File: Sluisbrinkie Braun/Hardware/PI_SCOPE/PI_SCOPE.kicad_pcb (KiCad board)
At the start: 2 copper layers, 40 x 110 mm, 97 parts, among them J1 Eurorack Power, J10 CV4, J2 USB_C_Receptacle_USB2.0_16P, J3 CV1, J4 CV2, J5 CV3, J6 CV4, J7 CV1, J8 CV2, J9 CV3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

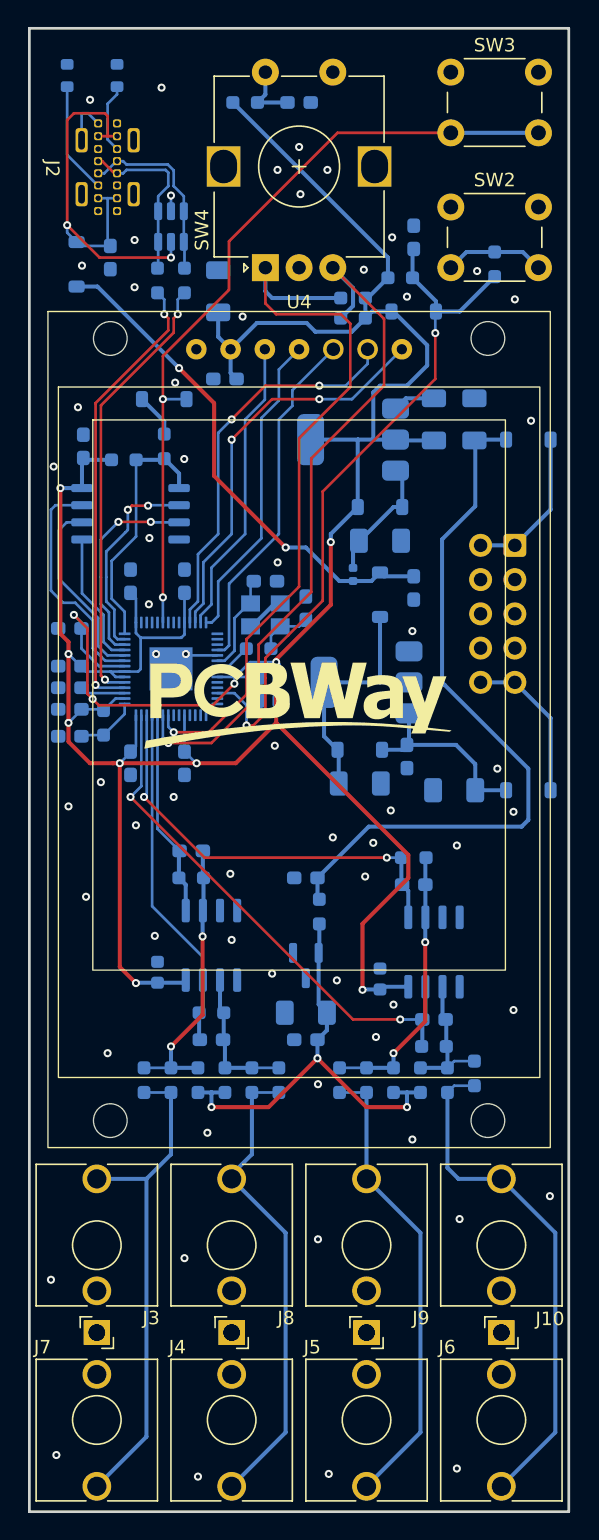
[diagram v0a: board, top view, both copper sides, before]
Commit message: [Braun] Several hardware fixes, move display from SPI1 to SPI0
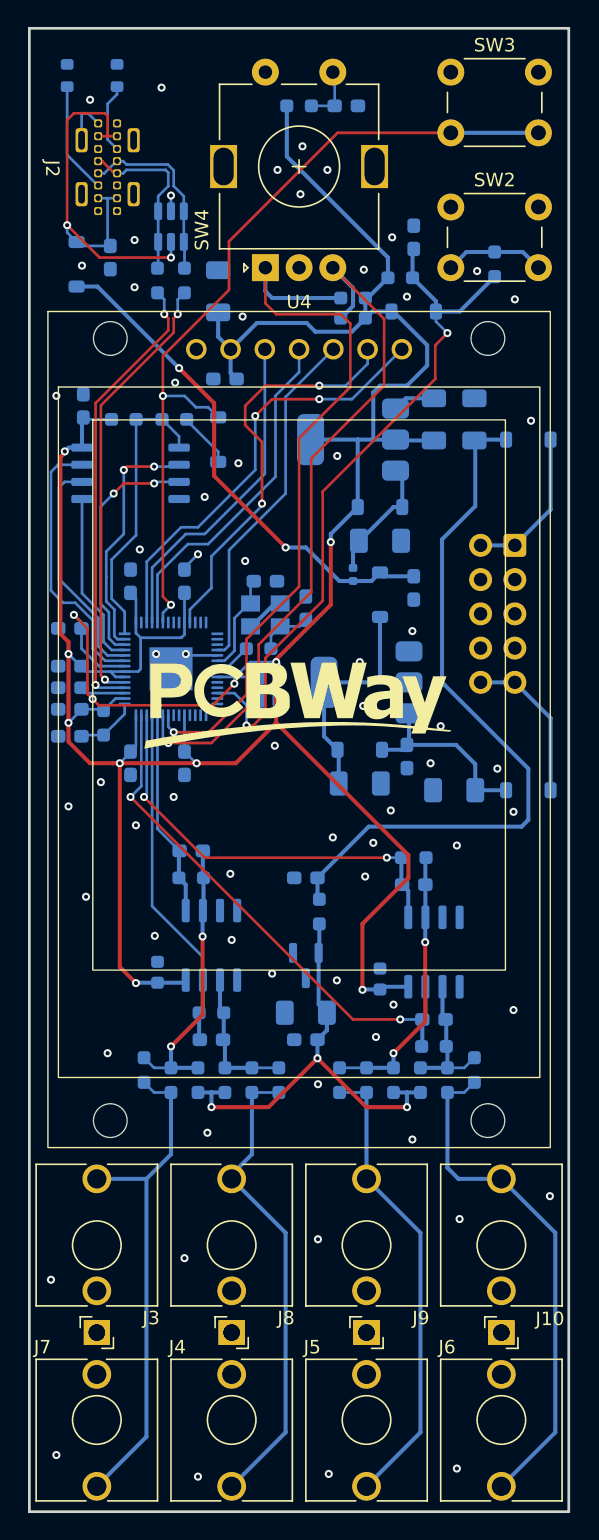
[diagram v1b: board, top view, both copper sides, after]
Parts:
- SW4: value PEC12R-3222F -> PEC11R-3222F; footprint Rotary_Encoder:RotaryEncoder_Alps_EC12E-Switch_Vertical_H20mm -> Rotary_Encoder:RotaryEncoder_Alps_EC11E-Switch_Vertical_H20mm
- moved D6 5.00 mm to (170.0, 57.0), turned to -90 degrees
- moved R24 4.01 mm to (176.0, 32.2)
- moved C32 3.51 mm to (179.5, 32.2)
- moved C15 3.00 mm to (160.0, 54.5)
- moved R20 3.00 mm to (163.0, 55.5)
- moved U9 3.00 mm to (163.5, 59.5)
- moved R21 2.14 mm to (166.8, 55.5), turned to 0 degrees
- moved R27 0.75 mm to (164.5, 103.8)
- moved R30 0.25 mm to (189.0, 103.8)
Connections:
- U8 pad 12: /CS -> unconnected-(U8-GPIO9-Pad12)
- U8 pad 13: /SCK -> unconnected-(U8-GPIO10-Pad13)
- U8 pad 14: /MOSI -> unconnected-(U8-GPIO11-Pad14)
- U8 pad 3: unconnected-(U8-GPIO1-Pad3) -> /CS
- U8 pad 4: unconnected-(U8-GPIO2-Pad4) -> /SCK
- U8 pad 5: unconnected-(U8-GPIO3-Pad5) -> /MOSI
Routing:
- net /USBBOOT: track 58.3 -> 61.8 mm
- net Net-(U8-QSPI_SD1): track 15.1 -> 18.2 mm
- net Net-(U8-QSPI_SCLK): track 14.0 -> 17.1 mm
- net Net-(U8-QSPI_SD0): track 10.1 -> 13.1 mm
- net Net-(U8-QSPI_SD3): track 17.3 -> 20.2 mm
- net Net-(U8-QSPI_SS): track 18.8 -> 21.6 mm
- net Net-(U8-QSPI_SD2): track 15.3 -> 17.9 mm
- net /SCK: track 22.2 -> 24.5 mm
- net /CS: track 30.1 -> 32.3 mm
- net /MOSI: track 23.4 -> 25.5 mm
- net GND: track 13.1 -> 14.7 mm, vias 63 -> 68
- net /DC: track 29.2 -> 30.2 mm
- net Net-(D6-A): track 3.27 -> 4.12 mm
- net +3V3: track 217.3 -> 218.1 mm
- net Net-(D5-A): track 51.7 -> 52.4 mm
